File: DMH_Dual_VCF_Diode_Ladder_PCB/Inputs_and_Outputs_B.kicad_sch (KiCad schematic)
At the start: 8 parts, among them J1 TS_Jack_6.35mm_Sw, J2 TS_Jack_6.35mm_Sw, J200 IDC_02x05, J3 TS_Jack_6.35mm_Sw, J4 TS_Jack_6.35mm_Sw, J5 TS_Jack_6.35mm_Sw, J50 Conn_01x06, J60 Conn_01x06

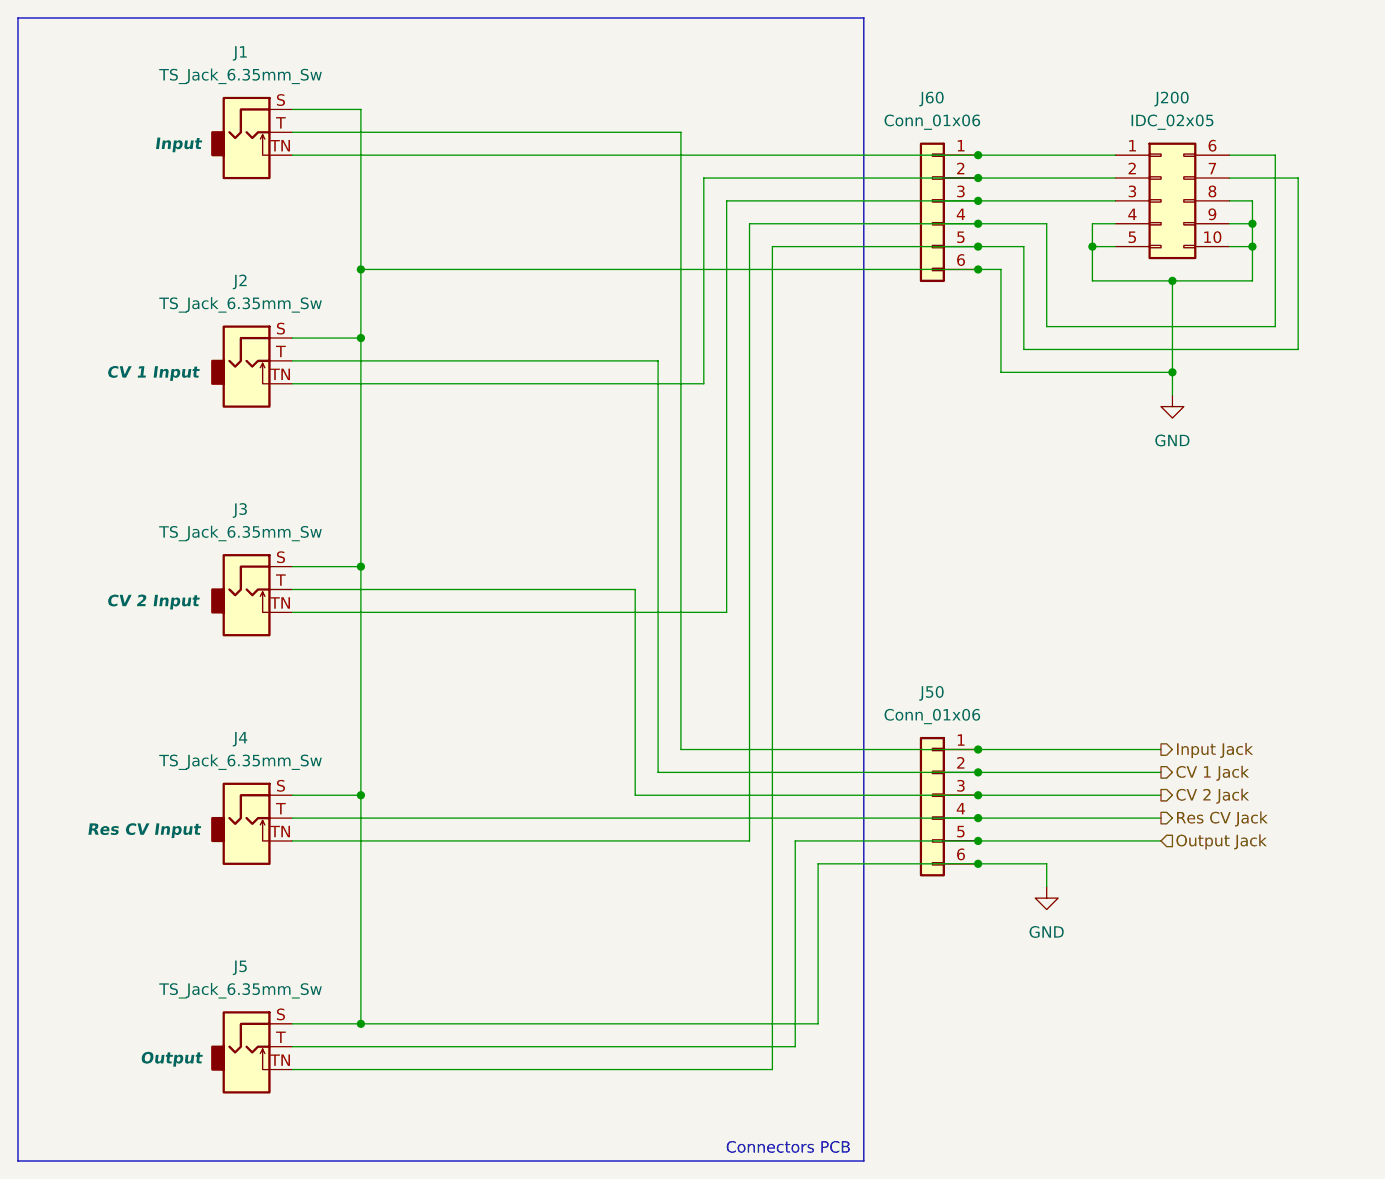
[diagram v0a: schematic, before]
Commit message: Started circuit schematic
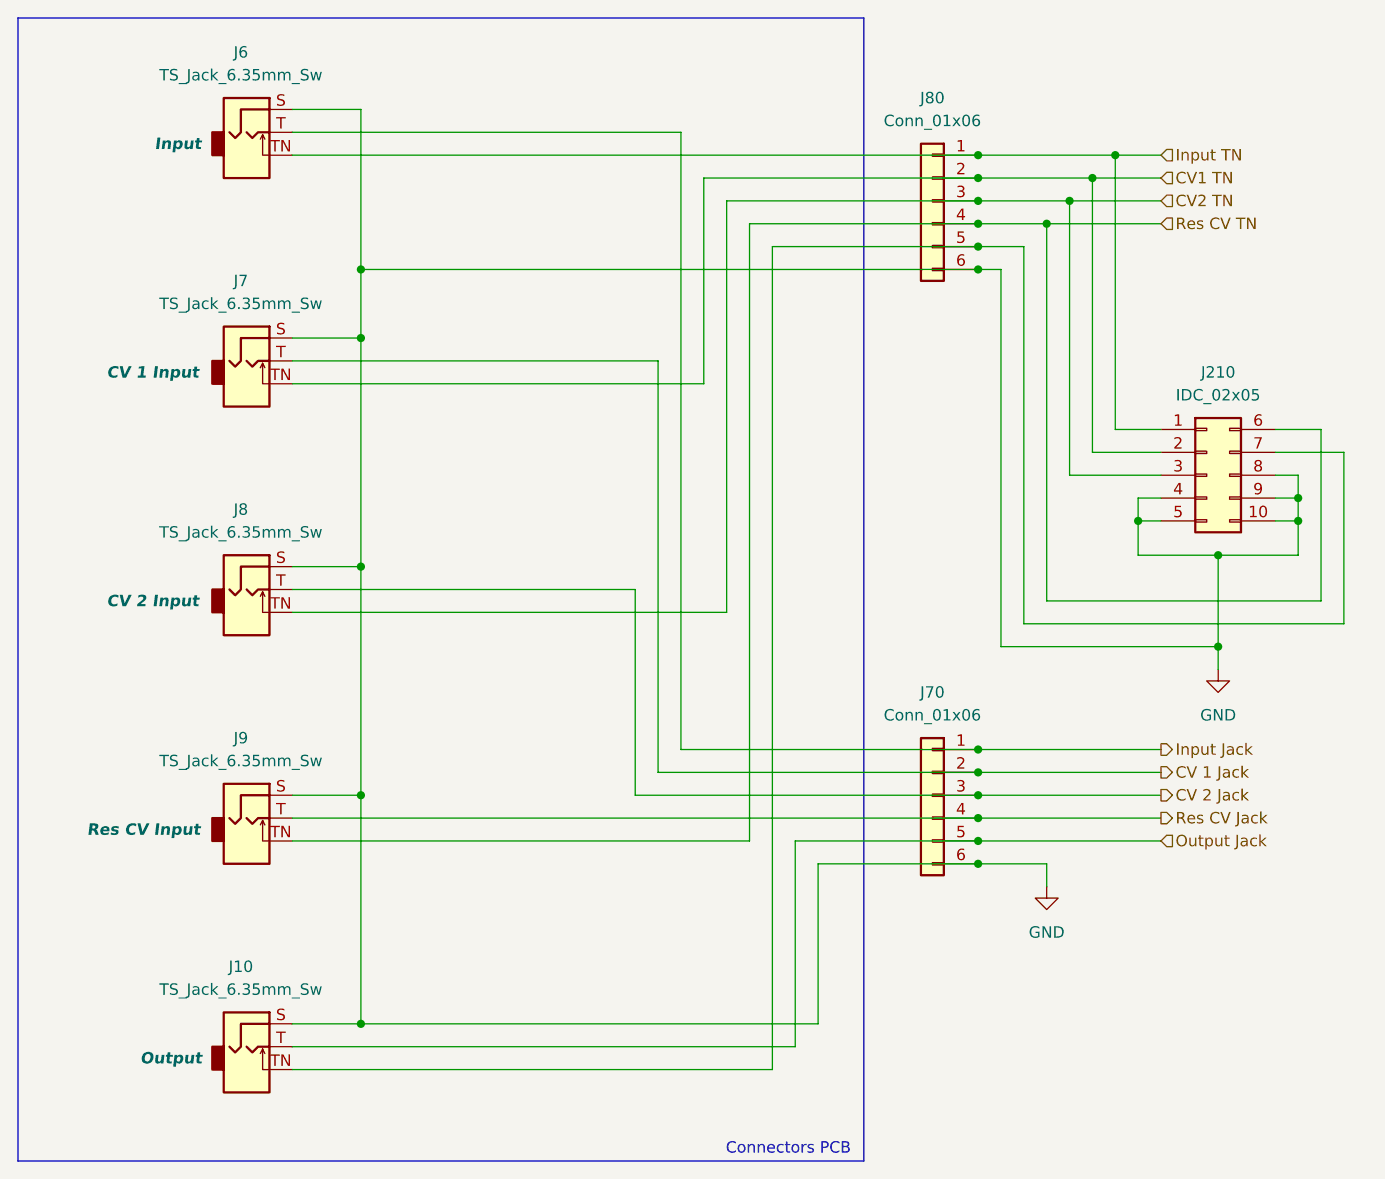
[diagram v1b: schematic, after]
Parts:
- renumbered J5 to J10, J200 to J210, J1 to J6, J2 to J7, J50 to J70, J3 to J8, J60 to J80, J4 to J9
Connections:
- net Input TN: now reaches J210.1 (Pin_1), J6.TN, J80.1 (Pin_1)
- net CV1 TN: now reaches J210.2 (Pin_2), J7.TN, J80.2 (Pin_2)
- net CV2 TN: now reaches J210.3 (Pin_3), J8.TN, J80.3 (Pin_3)
- net Res CV TN: now reaches J210.6 (Pin_6), J80.4 (Pin_4), J9.TN
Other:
- moved on the sheet: J210

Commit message: Concluded core and resonance circuits design
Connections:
- net GND: no longer J210.8 (Pin_8)
- no-connect marks 0 -> 1
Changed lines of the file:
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@@
-	)
-	(junction
-		(at 167.64 78.74)
-		(diameter 0)
-		(color 0 0 0 0)
 	)
 	(junction
@@
 		(color 0 0 0 0)
 	)
+	(no_connect
+		(at 165.1 76.2)
+	)
 	(wire
 		(pts
@@
 	(wire
 		(pts
-			(xy 165.1 76.2) (xy 167.64 76.2)
-		)
-		(stroke
-			(width 0)
-			(type default)
-		)
-	)
-	(wire
-		(pts
 			(xy 111.76 139.7) (xy 111.76 116.84)
 		)
@@
 		)
 		(stroke
-			(width 0)
-			(type default)
-		)
-	)
-	(wire
-		(pts
-			(xy 167.64 76.2) (xy 167.64 78.74)
-		)
-		(stroke

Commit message: Placed ICs and prepared passives
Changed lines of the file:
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@@
+		)
+	)
+	(rectangle
+		(start 132.08 62.23)
+		(end 175.26 104.14)
+		(stroke
+			(width 0)
+			(type default)
+		)
+		(fill
+			(type none)
 		)
 	)
@@
 		(exclude_from_sim no)
 		(at 110.998 151.13 0)
+		(effects
+			(font
+				(size 1.27 1.27)
+			)
+		)
+	)
+	(text "Connectors PCB"
+		(exclude_from_sim no)
+		(at 143.764 103.124 0)
 		(effects
 			(font
@@
 		(exclude_from_sim no)
 		(in_bom yes)
-		(on_board yes)
-		(dnp no)
-		(fields_autoplaced yes)
+		(on_board no)
+		(dnp no)
+		(fields_autoplaced yes)
